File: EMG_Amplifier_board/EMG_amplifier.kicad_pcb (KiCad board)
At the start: 2 copper layers, 50 x 28 mm, 55 parts, among them J1 Conn_01x04_Socket, J2 Conn_01x04_Pin, J3 Conn_01x06_Pin, J4 Conn_01x06_Socket, J7 Conn_01x06_Pin, U1 LPV821DBVR, U2 INA333xxDGK, U3 LPV821DBVR, U5 LPV821DBVR, U6 LPV821DBVR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

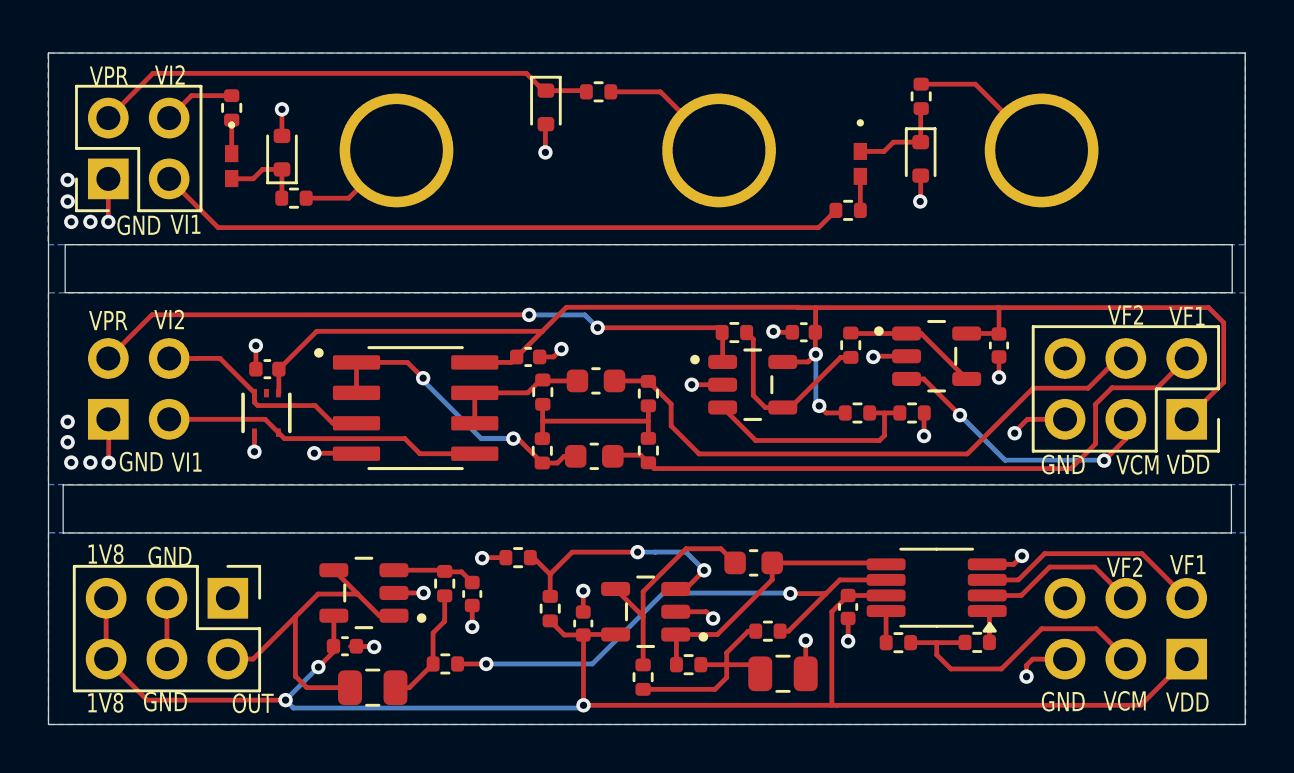
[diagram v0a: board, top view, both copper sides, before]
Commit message: update ferrite beads' and zener diodes' footprints
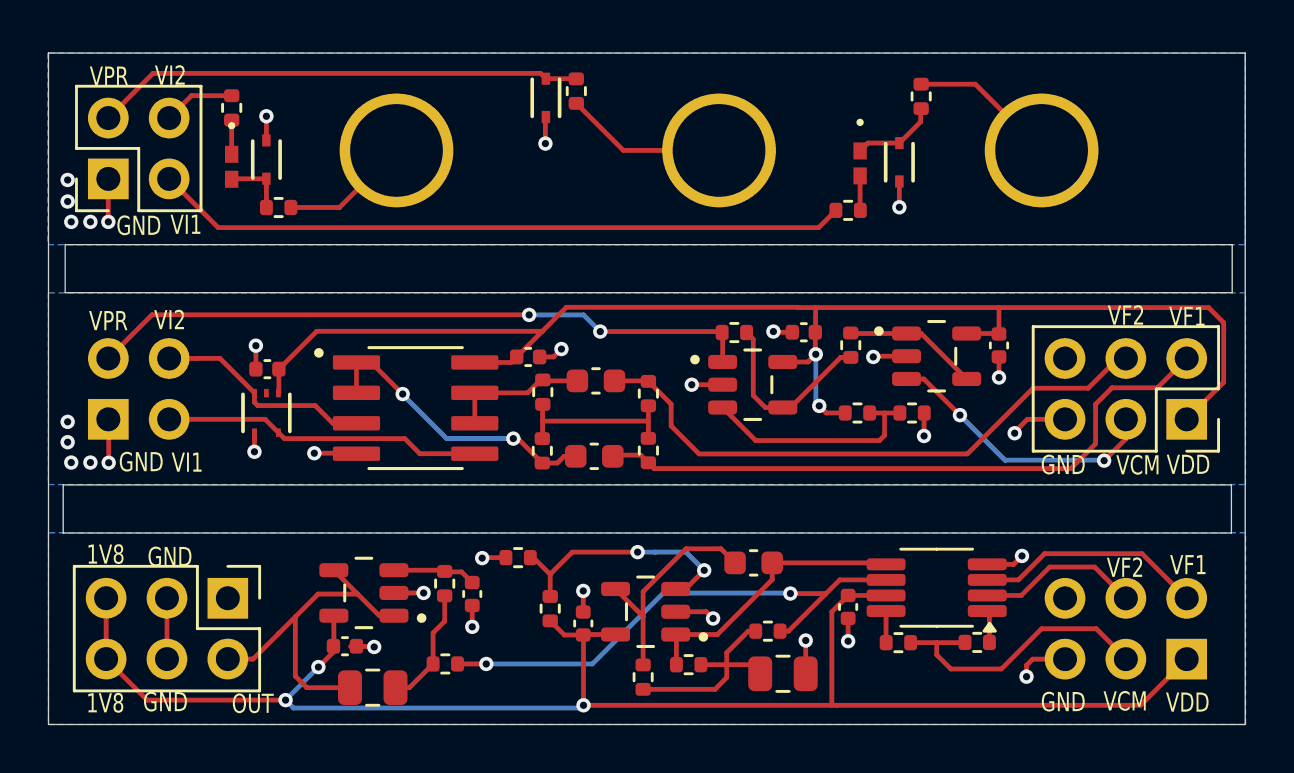
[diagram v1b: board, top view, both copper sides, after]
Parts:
- D1, D2, D3: value D_Zener -> ESD5Z2.5T1G; footprint Diode_SMD:D_SOD-523 -> ESD5Z2.5T1G:SOD-523_0P9X1P3_ONS
- L1, L2: footprint BLM15AX102SN1D_footprints:IND_BLM15_1P05X0P55X0P55_MUR -> BLM15AX102SN1D:IND_BLM15_1P05X0P55X0P55_MUR
- moved R5 0.93 mm to (34.0, 13.6), turned to 90 degrees
- moved D1 0.90 mm to (47.5, 16.6)
- moved R2 0.75 mm to (21.6, 18.4)
- moved D2 0.71 mm to (21.1, 16.4)
- moved D3 0.40 mm to (32.8, 13.9)
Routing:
- net /Electrode_Board/V_ER: track 5.97 -> 7.13 mm
- net Net-(D2-CATHODE): track 3.46 -> 2.65 mm
- net /Electrode_Board/V_E2: track 4.76 -> 5.56 mm
- net /Electrode_Board/V_PR: track 21.1 -> 20.4 mm

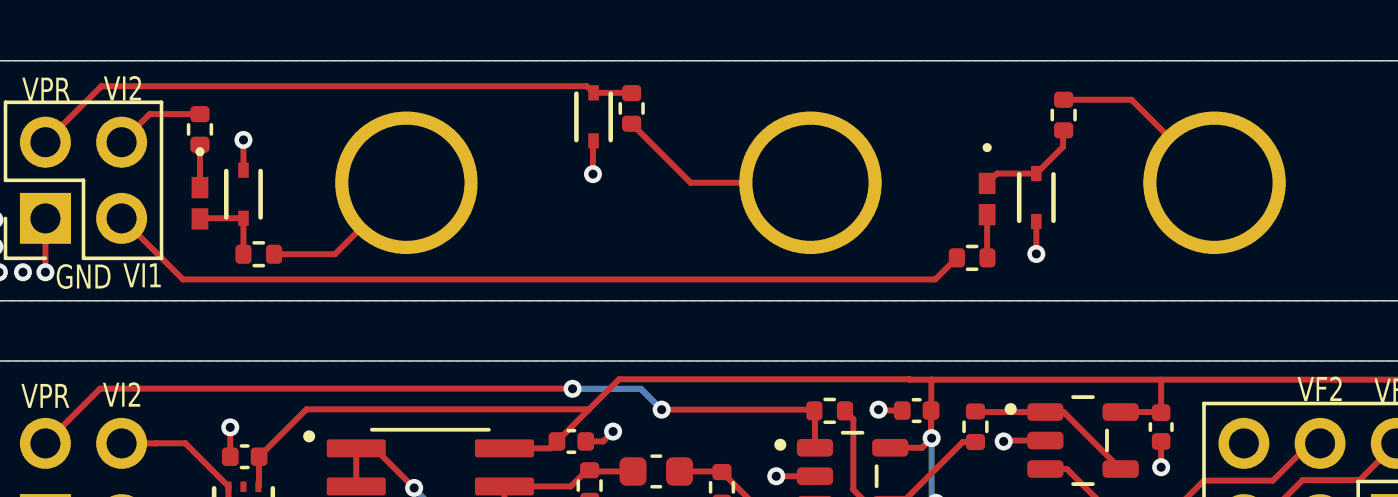
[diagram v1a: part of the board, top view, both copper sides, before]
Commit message: modify layout to add space around electrodes
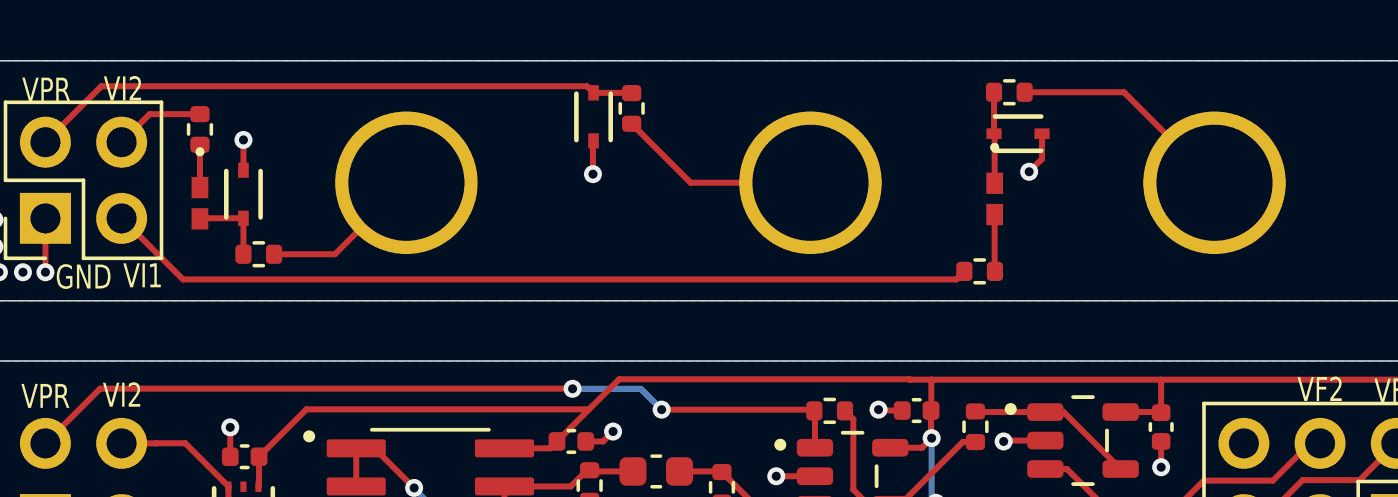
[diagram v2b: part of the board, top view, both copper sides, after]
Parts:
- moved D1 2.22 mm to (46.9, 14.4), turned to 0 degrees
- moved R1 1.96 mm to (46.6, 13.1), turned to 180 degrees
- moved R3 0.51 mm to (45.6, 19.0)
- moved L1 0.25 mm to (46.1, 16.6)
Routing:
- net /Electrode_Board/V_E1: track 6.18 -> 7.59 mm
- net Net-(D1-CATHODE): track 3.59 -> 3.08 mm

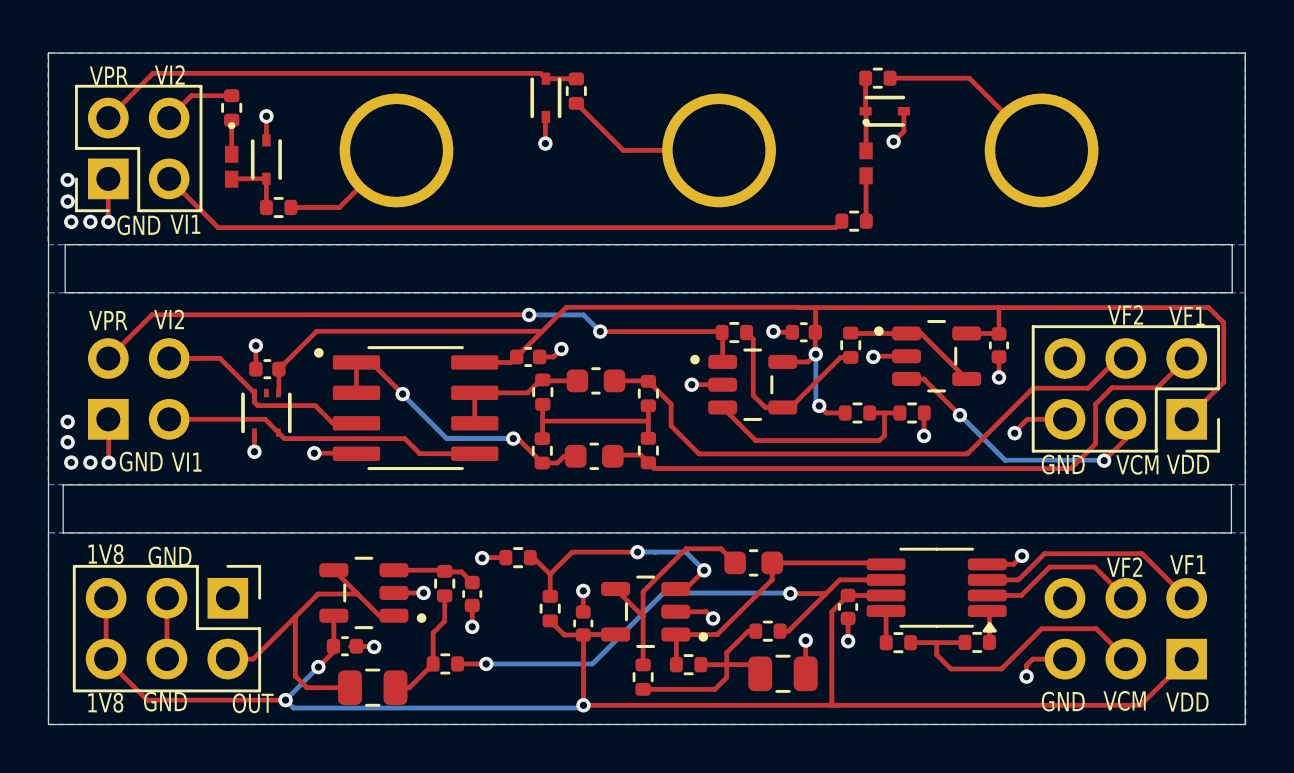
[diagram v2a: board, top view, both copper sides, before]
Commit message: minor spacing changes
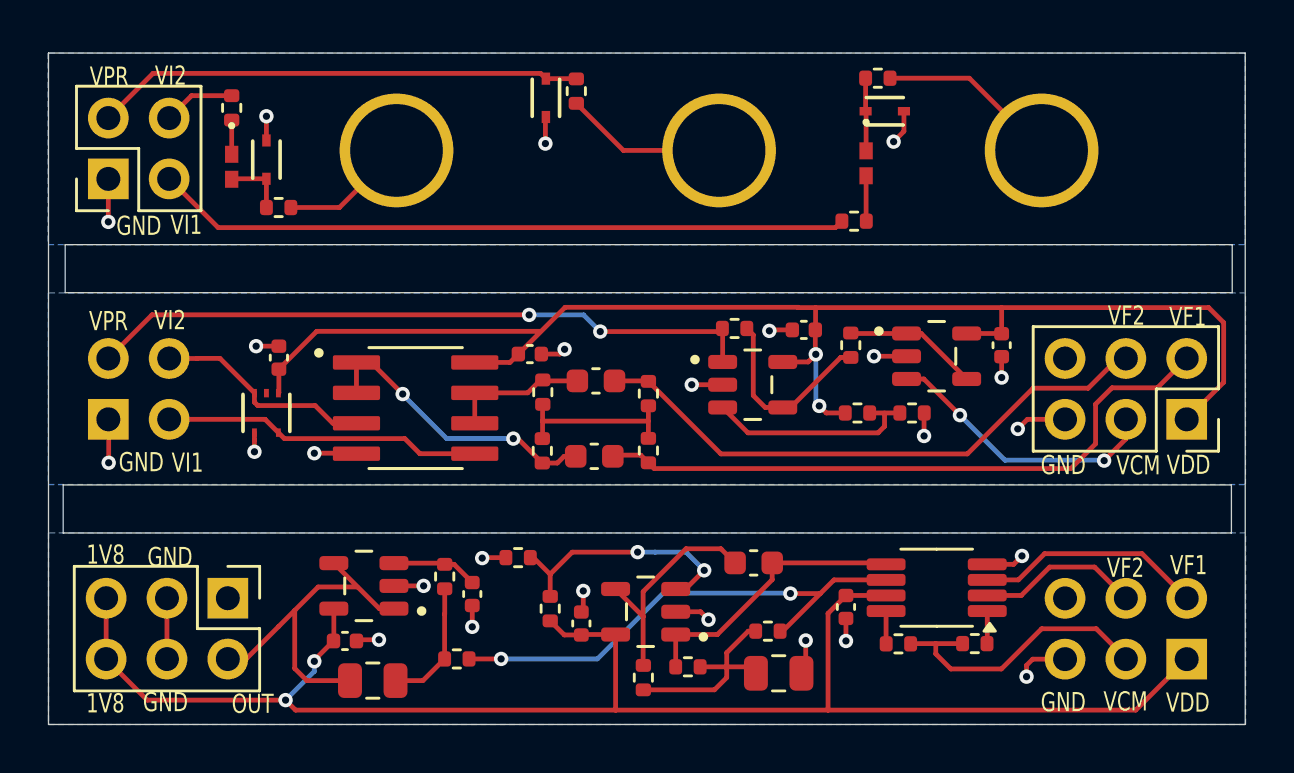
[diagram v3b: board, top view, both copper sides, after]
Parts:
- moved C12 0.68 mm to (21.6, 24.7), turned to -90 degrees
- moved R22 0.52 mm to (29.1, 37.3)
- moved C10 0.30 mm to (25.5, 38.2)
- moved R23 0.30 mm to (28.5, 33.9)
- moved U1 0.30 mm to (25.2, 34.2)
- moved C23 0.22 mm to (24.4, 36.5)
- moved C4 0.18 mm to (42.5, 37.9)
- moved R16 0.17 mm to (40.6, 23.5)
- moved C20 0.14 mm to (32.1, 24.6)
- moved R13 0.11 mm to (50.7, 36.7)
- moved C22 0.11 mm to (51.8, 24.2)
- moved C21 0.10 mm to (43.5, 23.6)
- moved R11 0.09 mm to (38.7, 37.6)
- moved C25 0.09 mm to (45.3, 35.1)
- moved C24 0.08 mm to (34.2, 35.8)
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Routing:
- net /Processing_Board/LPF_400Hz/V_EMG_INA: track 21.9 -> 21.1 mm
- net /Filtering_Board/V_F2: track 24.9 -> 24.4 mm
- net +1V8: track 66.3 -> 66.8 mm, vias 3 -> 2
- net GND: track 34.7 -> 34.5 mm, vias 33 -> 25

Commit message: switch LPV821 footprint package to SOT-23-5
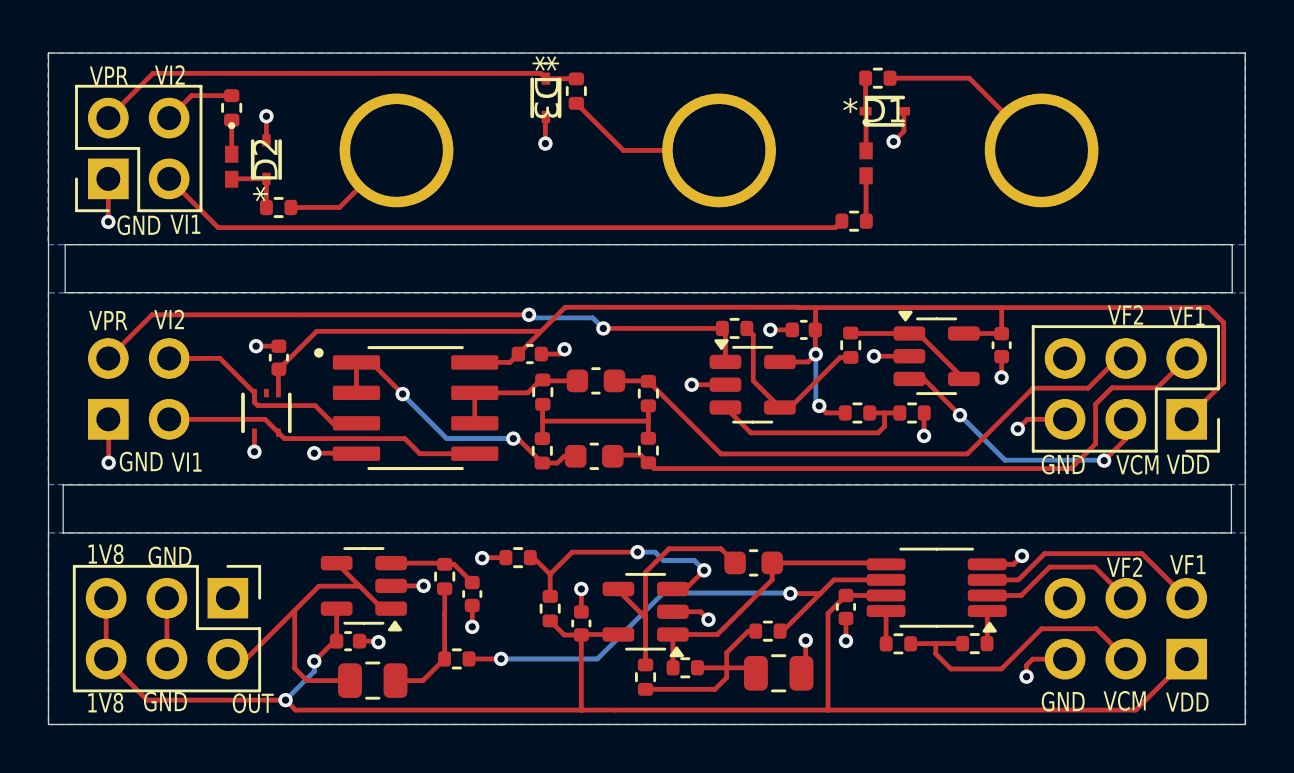
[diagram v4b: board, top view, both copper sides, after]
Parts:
- U1, U3, U5, U6: footprint LPV821DBVR:SOT95P280X145-5N -> Package_TO_SOT_SMD:SOT-23-5
- moved C23 0.13 mm to (24.5, 36.6)
- moved R11 0.12 mm to (38.6, 37.7)
- moved R12 0.09 mm to (36.9, 38.1)

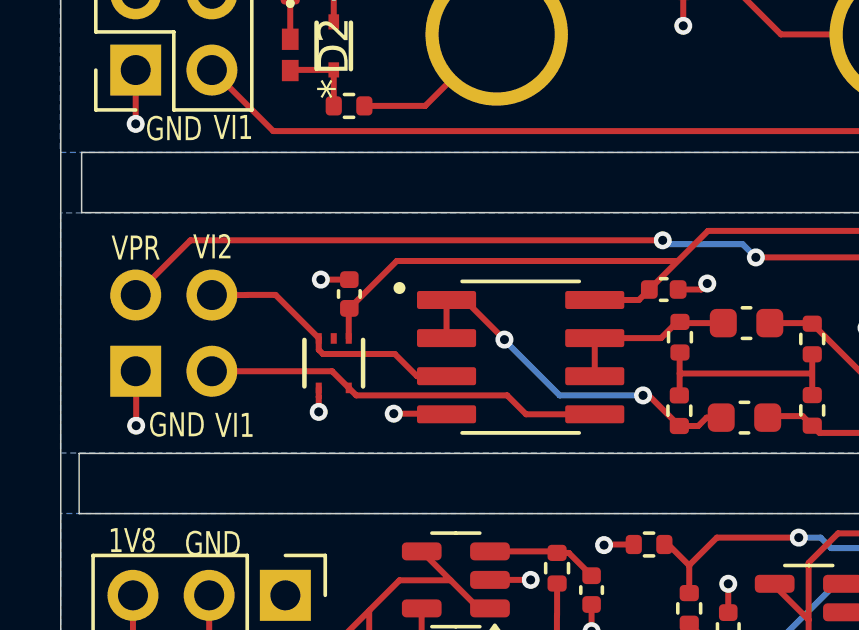
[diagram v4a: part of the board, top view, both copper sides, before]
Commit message: add MCU and BLE to main board schematic
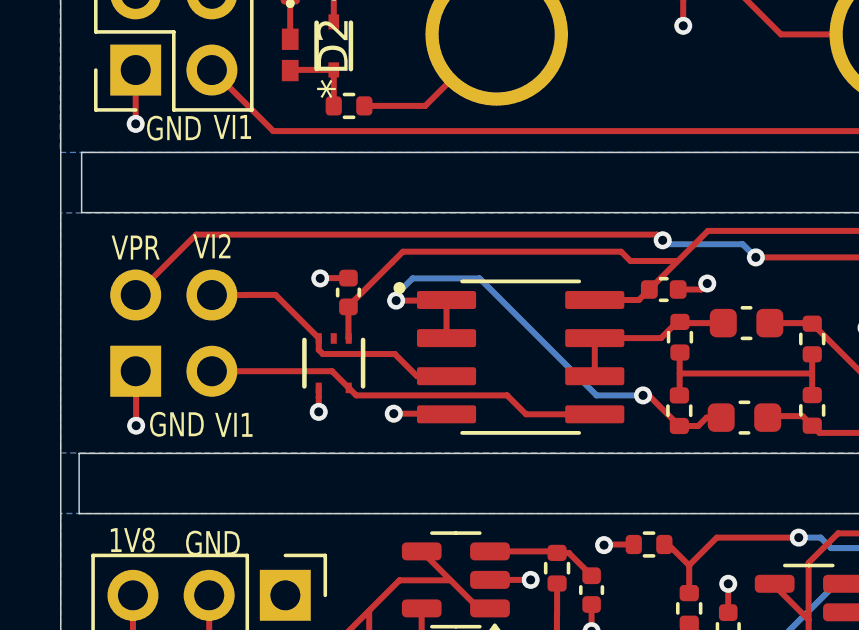
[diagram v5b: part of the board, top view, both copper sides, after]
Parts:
- moved C12 0.06 mm to (21.6, 24.7)
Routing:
- net Net-(U8--INA): track 12.3 -> 16.4 mm
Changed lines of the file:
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@@
 	(footprint "Capacitor_SMD:C_0402_1005Metric"
 		(layer "F.Cu")
-		(at 21.62 24.72 -90)
+		(at 21.59 24.67 -90)
 		(descr "Capacitor SMD 0402 (1005 Metric), square (rectangular) end terminal, IPC_7351 nominal, (Body size source: IPC-SM-782 page 76, https://www.pcb-3d.com/wordpress/wp-content/uploads/ipc-sm-782a_amendment_1_and_2.pdf), generated with kicad-footprint-generator")
 		(tags "capacitor")
@@
 	)
 	(segment
+		(start 20.66 24.19)
+		(end 21.59 24.19)
+		(width 0.2)
+		(layer "F.Cu")
+		(net 1)
+	)
+	(segment
 		(start 39.56 35.66)
 		(end 39.23 35.33)
@@
 	)
 	(segment
-		(start 21.62 24.24)
-		(end 20.67 24.24)
-		(width 0.2)
-		(layer "F.Cu")
-		(net 1)
-	)
-	(segment
 		(start 40.2675 25.85)
 		(end 38.86 25.85)
@@
 	)
 	(segment
+		(start 20.65 24.2)
+		(end 20.66 24.19)
+		(width 0.2)
+		(layer "F.Cu")
+		(net 1)
+	)
+	(segment
 		(start 20.6 28.15)
 		(end 20.600002 28.149998)
@@
 	)
 	(via
-		(at 20.67 24.24)
+		(at 20.65 24.2)
 		(size 0.6)
 		(drill 0.3)
@@
 	)
 	(segment
+		(start 32.065 22.93)
+		(end 31.875 22.74)
+		(width 0.2)
+		(layer "F.Cu")
+		(net 21)
+	)
+	(segment
 		(start 35.17 23.5)
 		(end 40.14 23.5)
@@
 	)
 	(segment
-		(start 16.3234 22.93)
-		(end 14.4988 24.7546)
+		(start 40.2675 23.6275)
+		(end 40.2675 24.9)
 		(width 0.2)
 		(layer "F.Cu")
@@
 	)
 	(segment
-		(start 40.2675 23.6275)
-		(end 40.2675 24.9)
+		(start 16.5134 22.74)
+		(end 14.4988 24.7546)
 		(width 0.2)
 		(layer "F.Cu")
@@
 	)
 	(segment
-		(start 32.065 22.93)
-		(end 16.3234 22.93)
+		(start 31.875 22.74)
+		(end 16.5134 22.74)
 		(width 0.2)
 		(layer "F.Cu")
@@
 	)
 	(segment
-		(start 24.86 24.92)
-		(end 24.86 26.19)
+		(start 24.84 24.94)
+		(end 24.86 24.92)
 		(width 0.2)
 		(layer "F.Cu")
@@
 	)
 	(segment
-		(start 25.47 24.92)
-		(end 24.86 24.92)
+		(start 24.86 24.92)
+		(end 24.86 26.19)
 		(width 0.2)
 		(layer "F.Cu")
@@
 	)
 	(segment
-		(start 26.79 26.24)
-		(end 25.47 24.92)
+		(start 31.41 28.1)
+		(end 31.6 28.1)
 		(width 0.2)
 		(layer "F.Cu")
@@
 	)
 	(segment
-		(start 31.41 28.1)
-		(end 31.6 28.1)
+		(start 33.25 29.12)
+		(end 33.53 28.84)
 		(width 0.2)
 		(layer "F.Cu")
@@
 	)
 	(segment
-		(start 33.25 29.12)
-		(end 33.53 28.84)
+		(start 23.18 24.94)
+		(end 24.84 24.94)
 		(width 0.2)
 		(layer "F.Cu")
@@
 	)
 	(via
-		(at 26.79 26.24)
+		(at 23.18 24.94)
 		(size 0.6)
 		(drill 0.3)
@@
 	)
 	(segment
-		(start 28.63 28.1)
+		(start 23.73 24.2)
+		(end 25.96 24.2)
+		(width 0.2)
+		(layer "B.Cu")
+		(net 32)
+	)
+	(segment
+		(start 29.86 28.1)
 		(end 31.41 28.1)
 		(width 0.2)
@@
 	)
 	(segment
-		(start 28.63 28.1)
-		(end 26.79 26.26)
+		(start 23.18 24.75)
+		(end 23.73 24.2)
+		(width 0.2)
+		(layer "B.Cu")
+		(net 32)
+	)
+	(segment
+		(start 23.18 24.94)
+		(end 23.18 24.75)
 		(width 0.2)
 		(layer "B.Cu")
@@
 	)
 	(segment
-		(start 26.79 26.26)
-		(end 26.79 26.24)
+		(start 25.96 24.2)
+		(end 29.86 28.1)
 		(width 0.2)
 		(layer "B.Cu")
@@
 	)
 	(segment
+		(start 23.04 23.676134)
+		(end 21.59 25.126134)
+		(width 0.2)
+		(layer "F.Cu")
+		(net 38)
+	)
+	(segment
 		(start 44.03 22.63)
 		(end 43.313 22.63)
@@
 	)
 	(segment
+		(start 30.99 23.62)
+		(end 30.68 23.31)
+		(width 0.2)
+		(layer "F.Cu")
+		(net 38)
+	)
+	(segment
 		(start 44.04 24.58)
 		(end 44.02 24.56)
@@
 	)
 	(segment
+		(start 21.59 25.15)
+		(end 21.59 26.191398)
+		(width 0.2)
+		(layer "F.Cu")
+		(net 38)
+	)
+	(segment
 		(start 44.48 27.03)
 		(end 45.27 27.03)
@@
 	)
 	(segment
+		(start 21.59 26.191398)
+		(end 21.6 26.201398)
+		(width 0.2)
+		(layer "F.Cu")
+		(net 38)
+	)
+	(segment
 		(start 44.03 23.55)
 		(end 44.03 22.63)
@@
 	)
 	(segment
-		(start 21.62 25.2)
-		(end 21.6 25.22)
+		(start 51.8 23.72)
+		(end 51.8 22.63)
 		(width 0.2)
 		(layer "F.Cu")
@@
 	)
 	(segment
-		(start 51.8 23.72)
-		(end 51.8 22.63)
+		(start 43.72 24.9)
+		(end 42.5425 24.9)
 		(width 0.2)
 		(layer "F.Cu")
@@
 	)
 	(segment
-		(start 43.72 24.9)
-		(end 42.5425 24.9)
+		(start 21.59 25.126134)
+		(end 21.59 25.15)
 		(width 0.2)
 		(layer "F.Cu")
@@
 	)
 	(segment
-		(start 23.2 23.62)
-		(end 21.62 25.2)
+		(start 30.68 23.31)
+		(end 23.406134 23.31)
 		(width 0.2)
 		(layer "F.Cu")
@@
 	)
 	(segment
-		(start 21.6 25.22)
-		(end 21.6 26.201398)
+		(start 44.185 26.735)
+		(end 44.48 27.03)
 		(width 0.2)
 		(layer "F.Cu")
@@
 	)
 	(segment
-		(start 44.185 26.735)
-		(end 44.48 27.03)
+		(start 61.0718 25.7508)
+		(end 61.0718 23.2566)
 		(width 0.2)
 		(layer "F.Cu")
@@
 	)
 	(segment
-		(start 61.0718 25.7508)
-		(end 61.0718 23.2566)
+		(start 23.406134 23.31)
+		(end 23.04 23.676134)
+		(width 0.2)
+		(layer "F.Cu")
+		(net 38)
+	)
+	(segment
+		(start 32.52 23.62)
+		(end 30.99 23.62)
 		(width 0.2)
 		(layer "F.Cu")
@@
 		(width 0.2)
 		(layer "F.Cu")
-		(net 38)
-	)
-	(segment
-		(start 32.52 23.62)
-		(end 23.2 23.62)
-		(width 0.2)
-		(layer "F.Cu")
